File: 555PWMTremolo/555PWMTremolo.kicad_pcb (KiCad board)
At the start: 2 copper layers, 56.4 x 96 mm, 37 parts

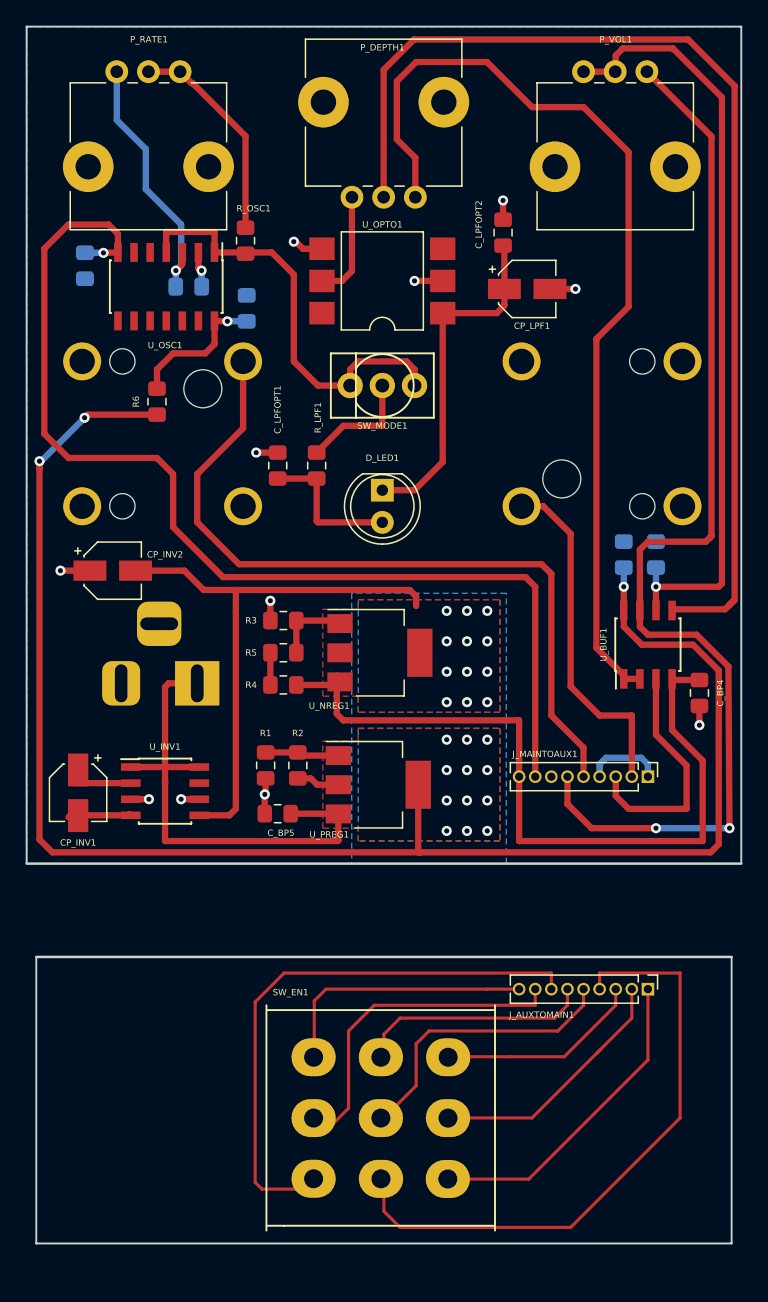
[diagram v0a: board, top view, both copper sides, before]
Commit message: Completed 555PWMTremolo Layout RevA
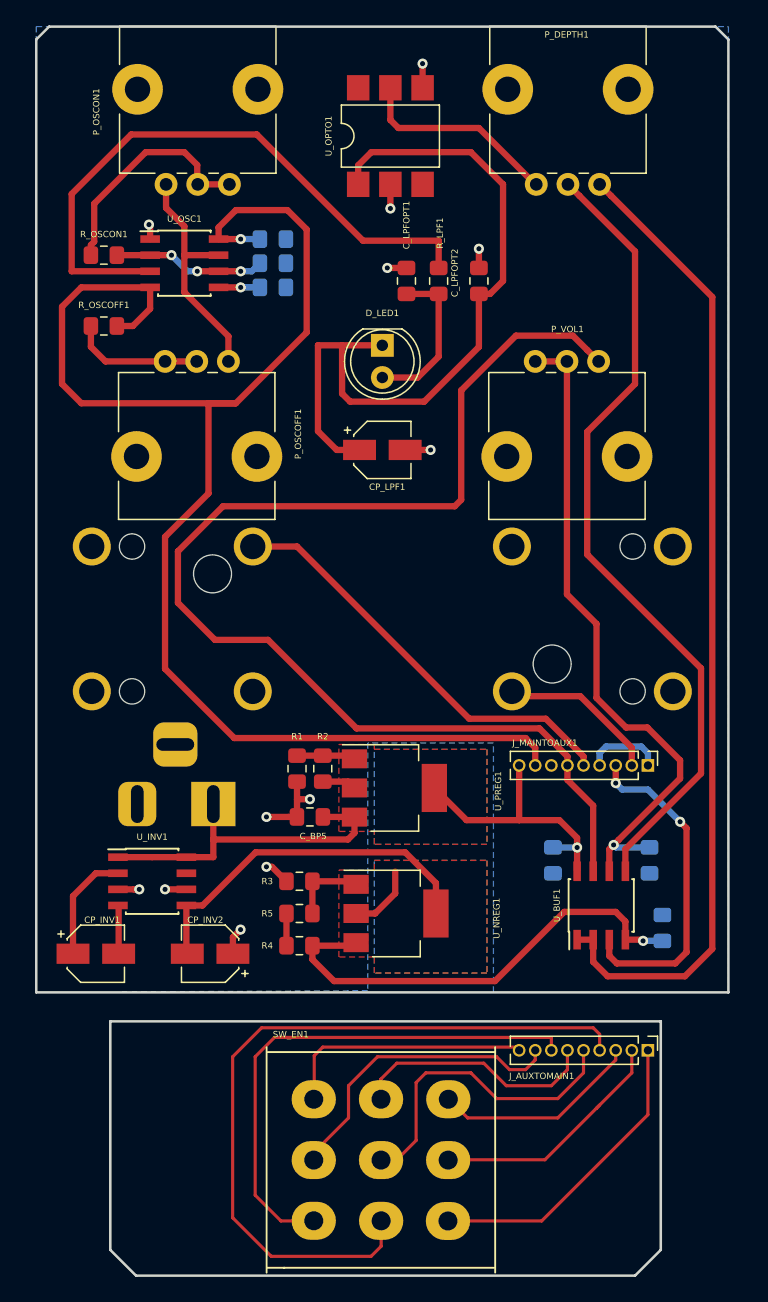
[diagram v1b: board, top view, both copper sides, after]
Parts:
- removed C_BP2: 100nF, Capacitor_SMD:C_0805_2012Metric_Pad1.15x1.40mm_HandSolder
- removed P_RATE1: B10K, Potentiometer_THT:Potentiometer_Alps_RK09L_Single_Vertical
- removed R6: 200R 1W, Resistor_SMD:R_0805_2012Metric_Pad1.15x1.40mm_HandSolder
- removed R_OSC1: 1K, Resistor_SMD:R_0805_2012Metric_Pad1.15x1.40mm_HandSolder
- removed SW_MODE1: SW_SPDT, DailywellSwitches:Dailywell_SPDT
- added C_OSC2: 100nF, Capacitor_SMD:C_0805_2012Metric_Pad1.15x1.40mm_HandSolder, B.Cu at (72.0, 91.9)
- added P_OSCOFF1: B10K, Potentiometer_THT:Potentiometer_Alps_RK09L_Single_Vertical, F.Cu at (63.5, 97.8)
- added P_OSCON1: B10K, Potentiometer_THT:Potentiometer_Alps_RK09L_Single_Vertical, F.Cu at (68.6, 83.8)
- added R_OSCOFF1: 100R, Resistor_SMD:R_0805_2012Metric_Pad1.15x1.40mm_HandSolder, F.Cu at (58.7, 95.0)
- added R_OSCON1: 100R, Resistor_SMD:R_0805_2012Metric_Pad1.15x1.40mm_HandSolder, F.Cu at (58.7, 89.4)
- CP_LPF1: value 10uF -> 22uF
- C_BP4: moved to B.Cu
- U_OPTO1: footprint Package_DIP:SMDIP-6_W9.53mm -> Package_DIP:SMDIP-6_W7.62mm
- U_OSC1: value 74HC7014 -> TLC555; footprint Package_SO:SOIC-14_3.9x8.7mm_P1.27mm -> Package_SO:SOIC-8_3.9x4.9mm_P1.27mm
- moved CP_INV2 31.2 mm to (67.1, 144.5), turned to 180 degrees
- moved C_BP3 24.8 mm to (94.1, 137.2), turned to 90 degrees
- moved R_GAIN1 24.1 mm to (101.7, 137.2), turned to 270 degrees
- moved P_VOL1 23.2 mm to (92.7, 97.8)
- moved U_BUF1 20.9 mm to (97.9, 140.7)
- moved R3 20.6 mm to (74.1, 138.8)
- moved R4 20.6 mm to (74.1, 143.9)
- moved R5 20.6 mm to (74.1, 141.4)
- moved U_NREG1 20.6 mm to (81.7, 141.4)
- moved C_BP4 18.8 mm to (102.7, 142.5), turned to 90 degrees
- moved C_LPFOPT1 17.8 mm to (82.5, 91.4)
- moved R_LPF1 17.5 mm to (85.1, 91.4)
- moved CP_LPF1 17.1 mm to (80.6, 104.8)
- moved J_IN1 14.6 mm to (97.0, 118.1)
- moved J_OUT1 14.6 mm to (64.3, 118.1)
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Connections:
- net /HexInverter_3PDT/3PDT_1_INT renamed /555PWMTremolo_3PDT/3PDT_1_INT
- net /HexInverter_3PDT/3PDT_2_INT renamed /555PWMTremolo_3PDT/3PDT_2_INT
- net /HexInverter_3PDT/3PDT_3_INT renamed /555PWMTremolo_3PDT/3PDT_3_INT
- net /HexInverter_3PDT/3PDT_4_INT renamed /555PWMTremolo_3PDT/3PDT_4_INT
- net /HexInverter_3PDT/3PDT_5_INT renamed /555PWMTremolo_3PDT/3PDT_5_INT
- net /HexInverter_3PDT/3PDT_6_INT renamed /555PWMTremolo_3PDT/3PDT_6_INT
- net /HexInverter_3PDT/3PDT_7_INT renamed /555PWMTremolo_3PDT/3PDT_7_INT
- net /HexInverter_3PDT/3PDT_8_INT renamed /555PWMTremolo_3PDT/3PDT_8_INT
- net /HexInverter_3PDT/3PDT_9_INT renamed /555PWMTremolo_3PDT/3PDT_9_INT
- net /HexInverter_Clock/CLK_OUT renamed /555PWMTremolo_Clock/CLK_OUT
- CP_INV2 pad 1: GND -> /GND
- CP_LPF1 pad 2: GND -> /GND
- C_BP1 pad 1: GND -> /3PDT_8_EXT
- C_BP1 pad 2: Net-(C_BP1-Pad2) -> /GND
- C_BP3 pad 1: GND -> /GND
- C_BP4 pad 2: GND -> /GND
- C_BP5 pad 1: GND -> /GND
- C_LPFOPT1 pad 2: GND -> /GND
- C_LPFOPT2 pad 2: GND -> /GND
- C_OSC1 pad 2: Net-(C_OSC1-Pad2) -> /GND
- J_IN1 pad 2: GND -> /GND
- J_IN1 pad 3: GND -> /GND
- J_IN1 pad 4: GND -> /GND
- J_MAINTOAUX1 pad 9: -5V -> +5V
- J_OUT1 pad 2: GND -> /GND
- J_OUT1 pad 3: GND -> /GND
- J_OUT1 pad 4: GND -> /GND
- J_PWR1 pad 2: GND -> /GND
- R1 pad 2: GND -> /GND
- R3 pad 2: GND -> /GND
- R_GAIN1 pad 2: GND -> /GND
- U_INV1 pad 3: GND -> /GND
- U_INV1 pad 6: GND -> /GND
- U_OPTO1 pad 2: GND -> /GND
- U_OPTO1 pad 4: GND -> /GND
- U_OSC1 pad 1: Net-(R_OSC1-Pad2) -> /GND
- U_OSC1 pad 2: Net-(C_OSC1-Pad2) -> Net-(C_OSC1-Pad1)
- U_OSC1 pad 3: Net-(C_OSC1-Pad1) -> Net-(R_LPF1-Pad2)
- U_OSC1 pad 4: Net-(R_OSC1-Pad2) -> /3PDT_8_EXT
- U_OSC1 pad 5: (no net) -> Net-(C_OSC2-Pad1)
- U_OSC1 pad 6: (no net) -> Net-(C_OSC1-Pad1)
- U_OSC1 pad 7: /3PDT_8_EXT -> Net-(P_OSCOFF1-Pad3)
- U_OSC1 pad 8: (no net) -> /3PDT_8_EXT
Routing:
- net +5V: track 131.0 -> 24.9 mm, vias 15 -> 1
- net Net-(R_LPF1-Pad2): track 9.23 -> 48.8 mm
- net Net-(R_OSC1-Pad2): track 34.3 -> 0.00 mm
- net Net-(CP_LPF1-Pad1): track 27.3 -> 60.9 mm
- net /3PDT_8_EXT: track 86.8 -> 119.0 mm
- net /3PDT_5_EXT: track 60.9 -> 33.7 mm
- net -5V: track 60.8 -> 37.0 mm, vias 0 -> 1
- net /GND: track 0.00 -> 23.8 mm, vias 0 -> 12
- net Net-(P_DEPTH1-Pad2): track 86.6 -> 64.1 mm
- net GND: track 21.0 -> 0.00 mm, vias 11 -> 0
- net Net-(P_OSCOFF1-Pad3): track 0.00 -> 18.7 mm
- net Net-(P_OSCON1-Pad1): track 0.00 -> 18.4 mm
- net Net-(P_RATE1-Pad2): track 17.0 -> 0.00 mm
- net /3PDT_2_EXT: track 27.4 -> 12.7 mm
- net +9V: track 40.1 -> 25.9 mm
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- added copper zone on B.Cu, net /GND
- removed copper zone on B.Cu, net GND
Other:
- board size 56.4 x 96 mm -> 54.6 x 98.6 mm

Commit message: Tidied up 555 layout
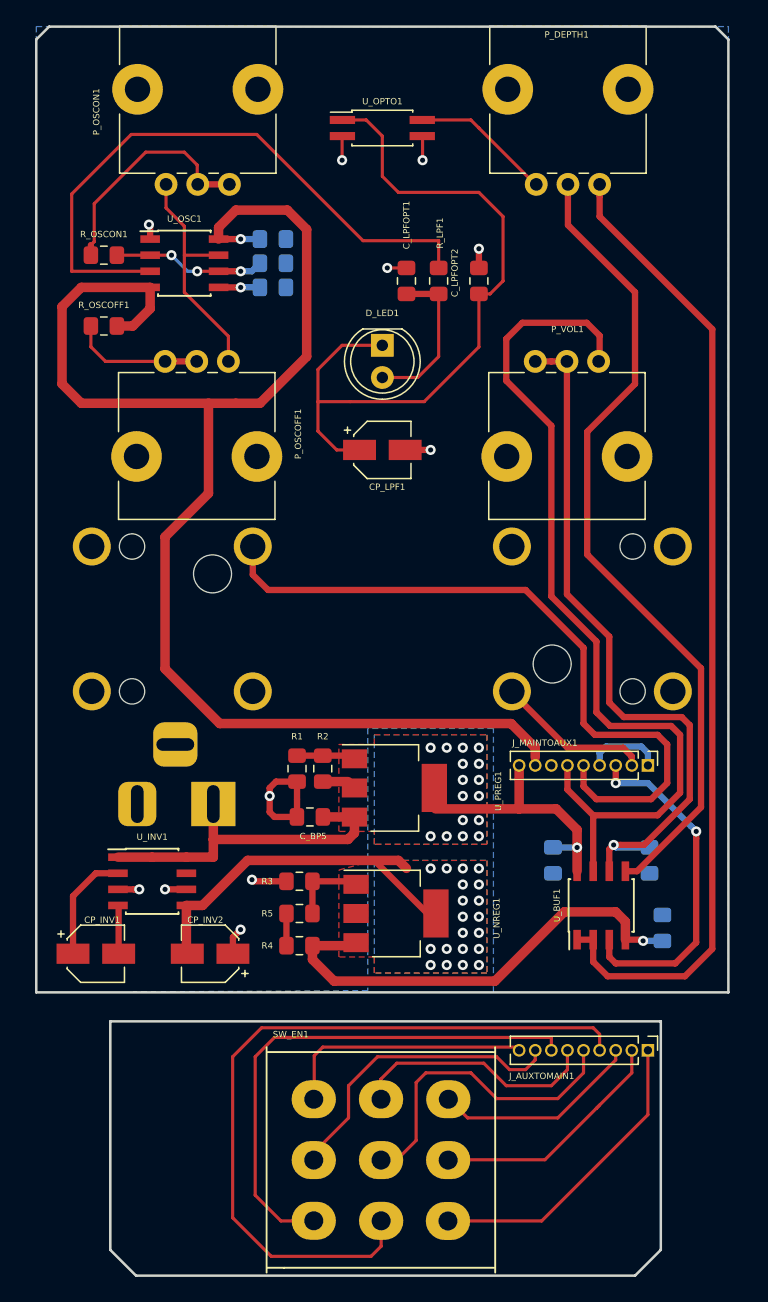
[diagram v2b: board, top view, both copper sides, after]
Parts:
- U_OPTO1: value 4N35 -> LTV-357T; footprint Package_DIP:SMDIP-6_W7.62mm -> Package_SO:SO-4_4.4x2.3mm_P1.27mm
- moved U_OPTO1 0.90 mm to (80.6, 79.4), turned to 0 degrees
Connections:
- U_OPTO1 pad 3: (no net) -> /GND
- U_OPTO1 pad 4: /GND -> /555PWMTremolo_Clock/CLK_OUT
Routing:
- net /3PDT_6_EXT: track 96.0 -> 71.6 mm
- net /3PDT_5_EXT: track 33.7 -> 56.2 mm
- net /555PWMTremolo_Clock/CLK_OUT: track 16.2 -> 11.1 mm
- net -9V: track 34.0 -> 29.4 mm, vias 0 -> 20
- net /GND: track 23.8 -> 27.7 mm, vias 12 -> 11
- net Net-(P_VOL1-Pad1): track 52.6 -> 56.4 mm
- net Net-(CP_LPF1-Pad1): track 60.9 -> 58.4 mm
- net /3PDT_8_EXT: track 119.0 -> 120.1 mm
- net /3PDT_3_EXT: track 26.2 -> 27.2 mm
- net Net-(P_DEPTH1-Pad2): track 64.1 -> 64.7 mm
- net +5V: track 24.9 -> 25.3 mm, vias 1 -> 17

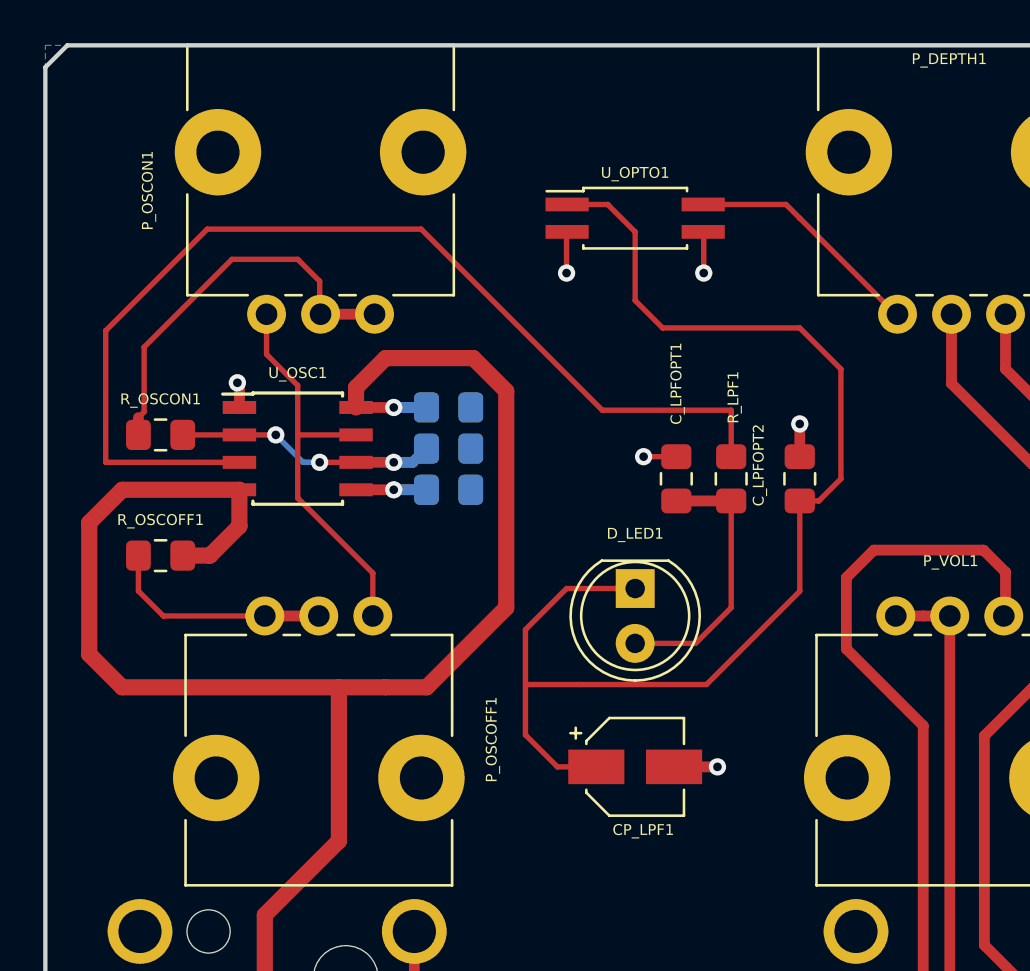
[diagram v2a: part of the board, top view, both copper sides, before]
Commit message: Tidied up 555 layout
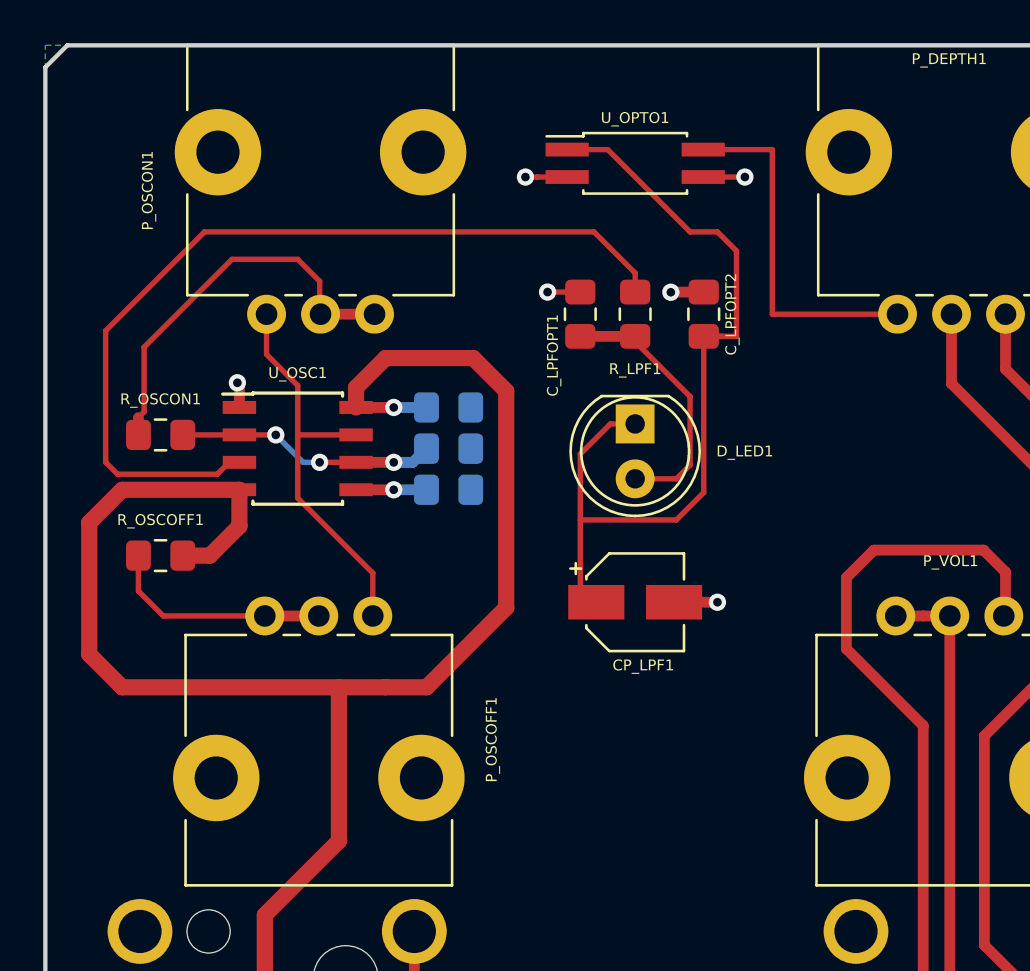
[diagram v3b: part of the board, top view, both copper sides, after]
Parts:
- moved C_LPFOPT2 8.82 mm to (83.8, 83.8)
- moved R_LPF1 8.82 mm to (80.6, 83.8)
- moved C_LPFOPT1 8.82 mm to (78.1, 83.8)
- moved CP_LPF1 7.62 mm to (80.6, 97.2)
- moved D_LED1 7.62 mm to (80.6, 88.9)
- moved U_OPTO1 2.54 mm to (80.6, 76.8)
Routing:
- net Net-(CP_LPF1-Pad1): track 58.4 -> 39.9 mm
- net Net-(R_LPF1-Pad2): track 48.8 -> 40.8 mm
- net /555PWMTremolo_Clock/CLK_OUT: track 11.1 -> 16.7 mm

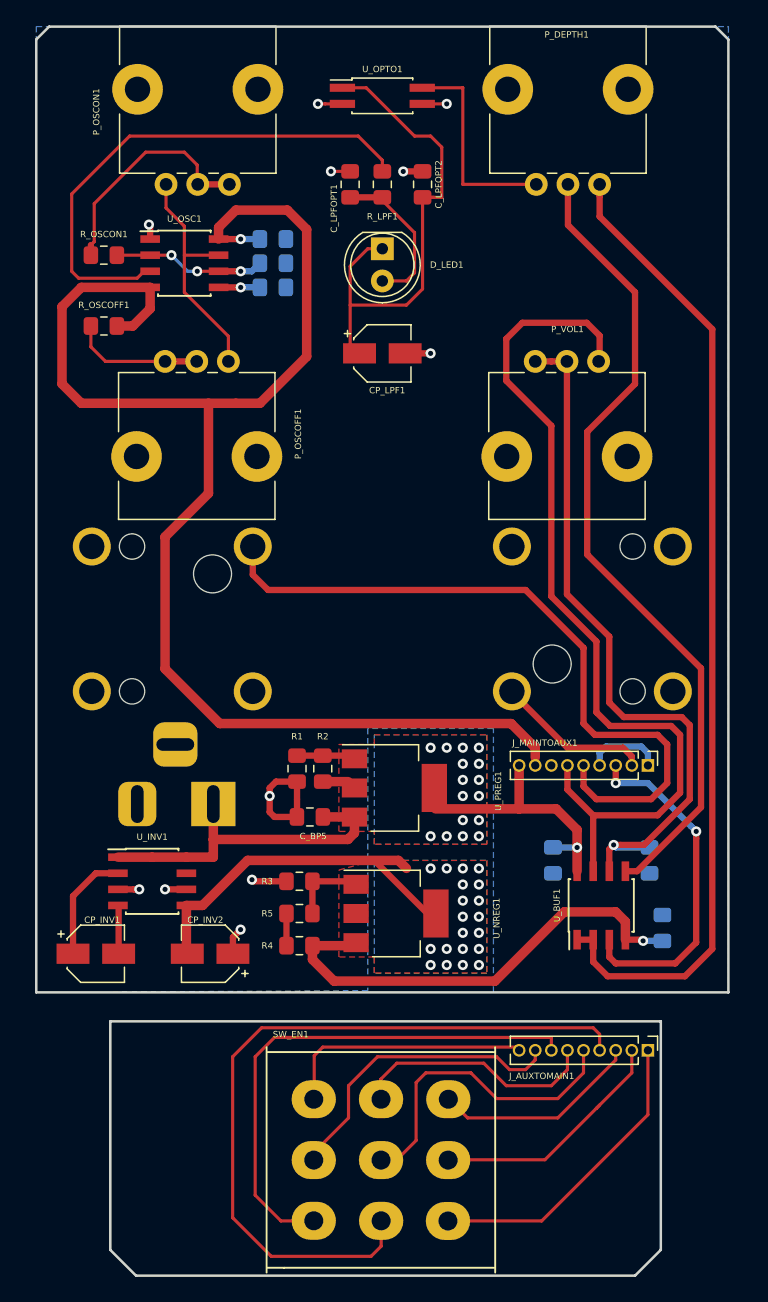
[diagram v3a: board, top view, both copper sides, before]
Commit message: Tidied up 555 layout
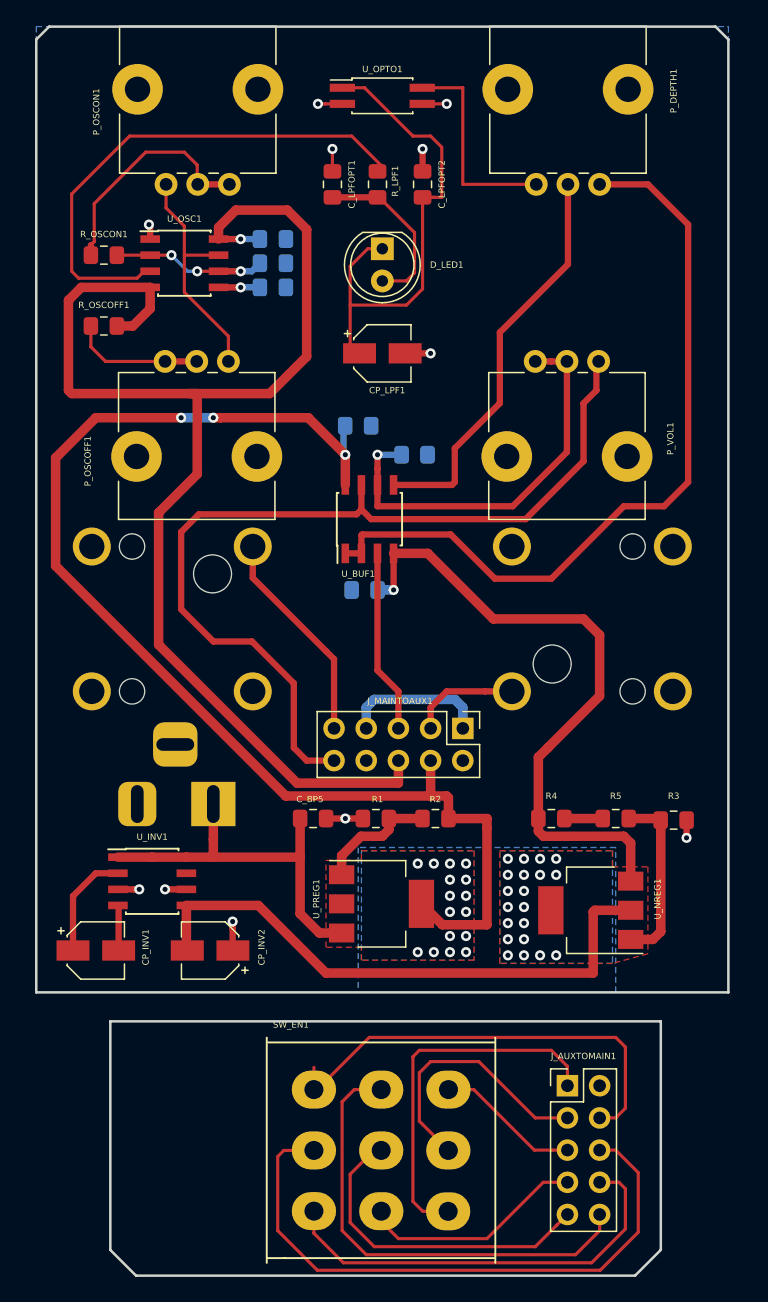
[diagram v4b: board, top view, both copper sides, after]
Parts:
- J_AUXTOMAIN1, J_MAINTOAUX1: value Conn_01x09 -> Conn_02x05_Counter_Clockwise; footprint Connector_PinHeader_1.27mm:PinHeader_1x09_P1.27mm_Vertical -> CustomHeaders:IDCHeader_02x05_P2.54mm_Vertical_Counter_Clockwise
- moved C_BP3 37.6 mm to (78.7, 102.9), turned to 180 degrees
- moved R_GAIN1 37.0 mm to (83.2, 105.2), turned to 0 degrees
- moved U_BUF1 35.5 mm to (79.6, 110.2)
- moved C_BP4 35.5 mm to (79.2, 115.8), turned to 180 degrees
- moved R3 29.9 mm to (103.6, 134.0), turned to 0 degrees
- moved R5 26.1 mm to (99.1, 133.9)
- moved R4 22.3 mm to (94.0, 133.9), turned to 180 degrees
- moved U_NREG1 15.4 mm to (97.1, 141.1), turned to 180 degrees
- moved J_MAINTOAUX1 14.9 mm to (87.0, 126.7)
- moved R2 9.72 mm to (84.8, 133.9), turned to 180 degrees
- moved U_PREG1 9.20 mm to (80.6, 140.6)
- moved R1 7.36 mm to (80.1, 133.9), turned to 180 degrees
- moved J_AUXTOMAIN1 6.94 mm to (95.2, 154.9), turned to 0 degrees
- moved C_LPFOPT1 1.40 mm to (76.7, 83.8)
- moved SW_EN1 0.76 mm to (80.5, 160.0)
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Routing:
- net +5V: track 25.3 -> 101.0 mm, vias 17 -> 19
- net /555PWMTremolo_3PDT/3PDT_4_INT: track 59.7 -> 17.9 mm
- net /3PDT_5_EXT: track 56.2 -> 17.3 mm
- net Net-(P_DEPTH1-Pad2): track 64.7 -> 32.1 mm
- net /555PWMTremolo_3PDT/3PDT_8_INT: track 23.7 -> 48.7 mm
- net Net-(P_VOL1-Pad1): track 56.4 -> 32.7 mm
- net -9V: track 29.4 -> 46.5 mm
- net /555PWMTremolo_3PDT/3PDT_6_INT: track 19.8 -> 36.8 mm
- net Net-(P_DEPTH1-Pad1): track 78.3 -> 61.7 mm
- net /555PWMTremolo_3PDT/3PDT_9_INT: track 20.0 -> 35.5 mm
- net -5V: track 37.0 -> 51.6 mm
- net /3PDT_3_EXT: track 27.2 -> 14.7 mm, vias 2 -> 0
- net /3PDT_8_EXT: track 120.1 -> 108.6 mm
- net Net-(R3-Pad1): track 6.08 -> 14.2 mm
- net /555PWMTremolo_3PDT/3PDT_7_INT: track 41.4 -> 33.8 mm
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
